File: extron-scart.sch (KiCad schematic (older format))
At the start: 6 parts, among them J1 SCART-F, J2 Conn_Coaxial, J3 Conn_Coaxial, J4 Conn_Coaxial, J5 Conn_Coaxial, J6 Conn_01x03_Male

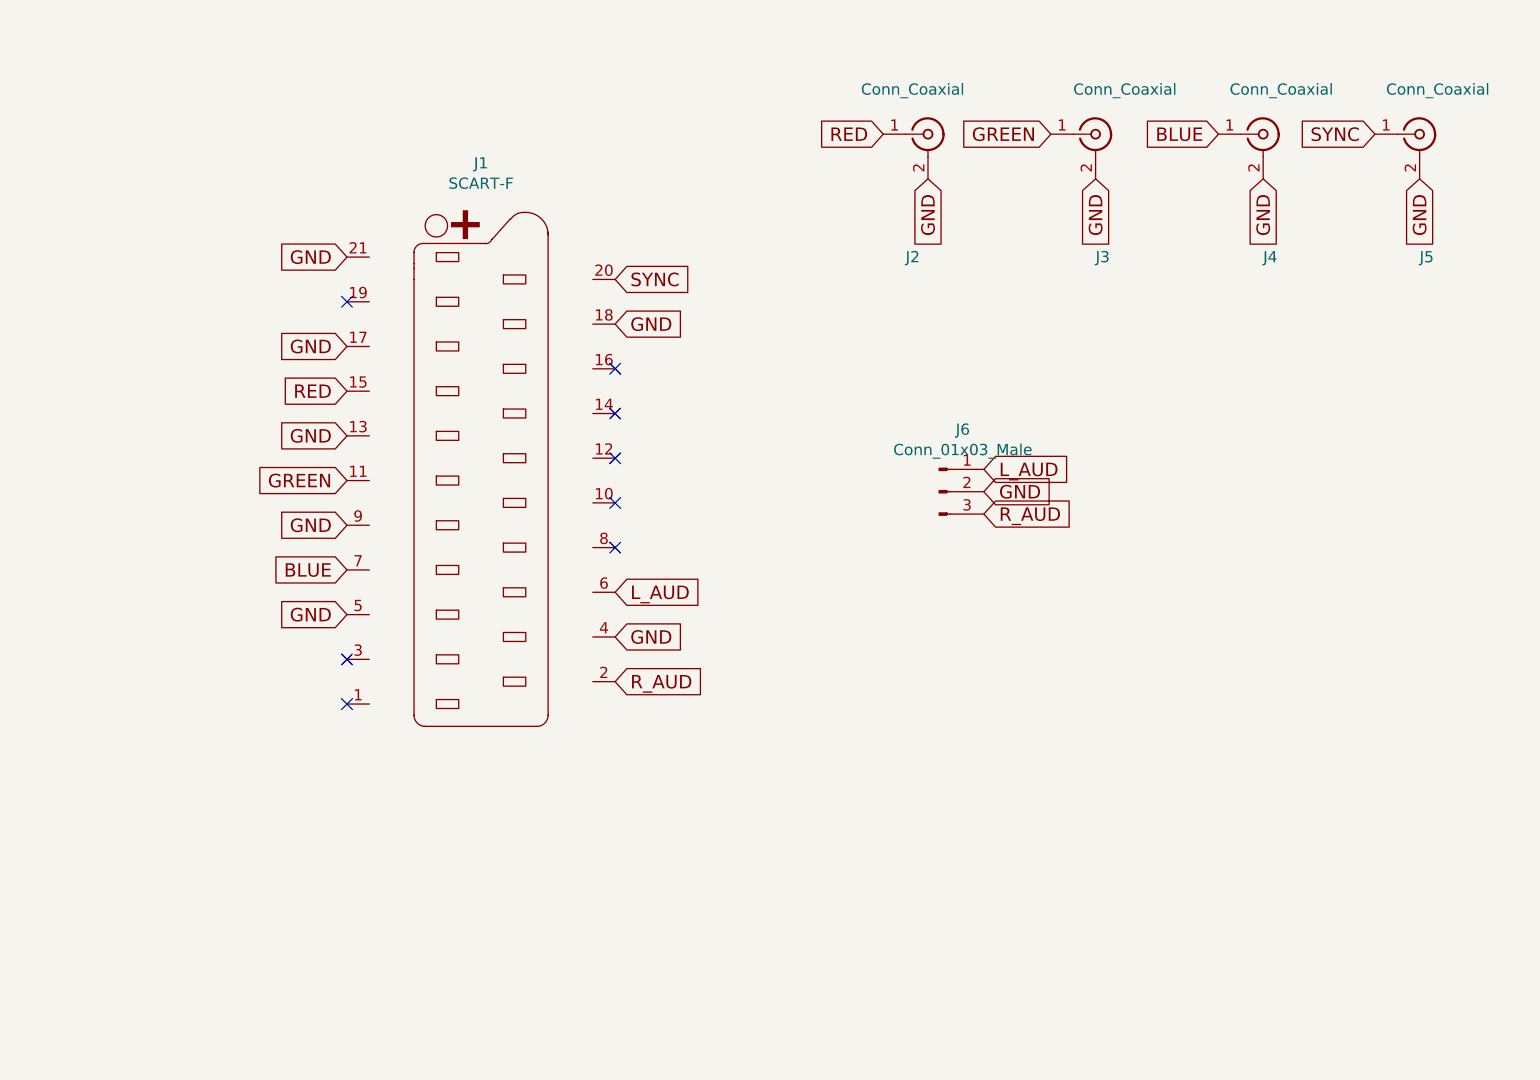
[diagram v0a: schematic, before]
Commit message: New sch/pcb input from extron crosspoint dimensions
Different orientation for the board
Added selectable sync stripper

Missing mounting holes, and better silkscreen, but mostly done
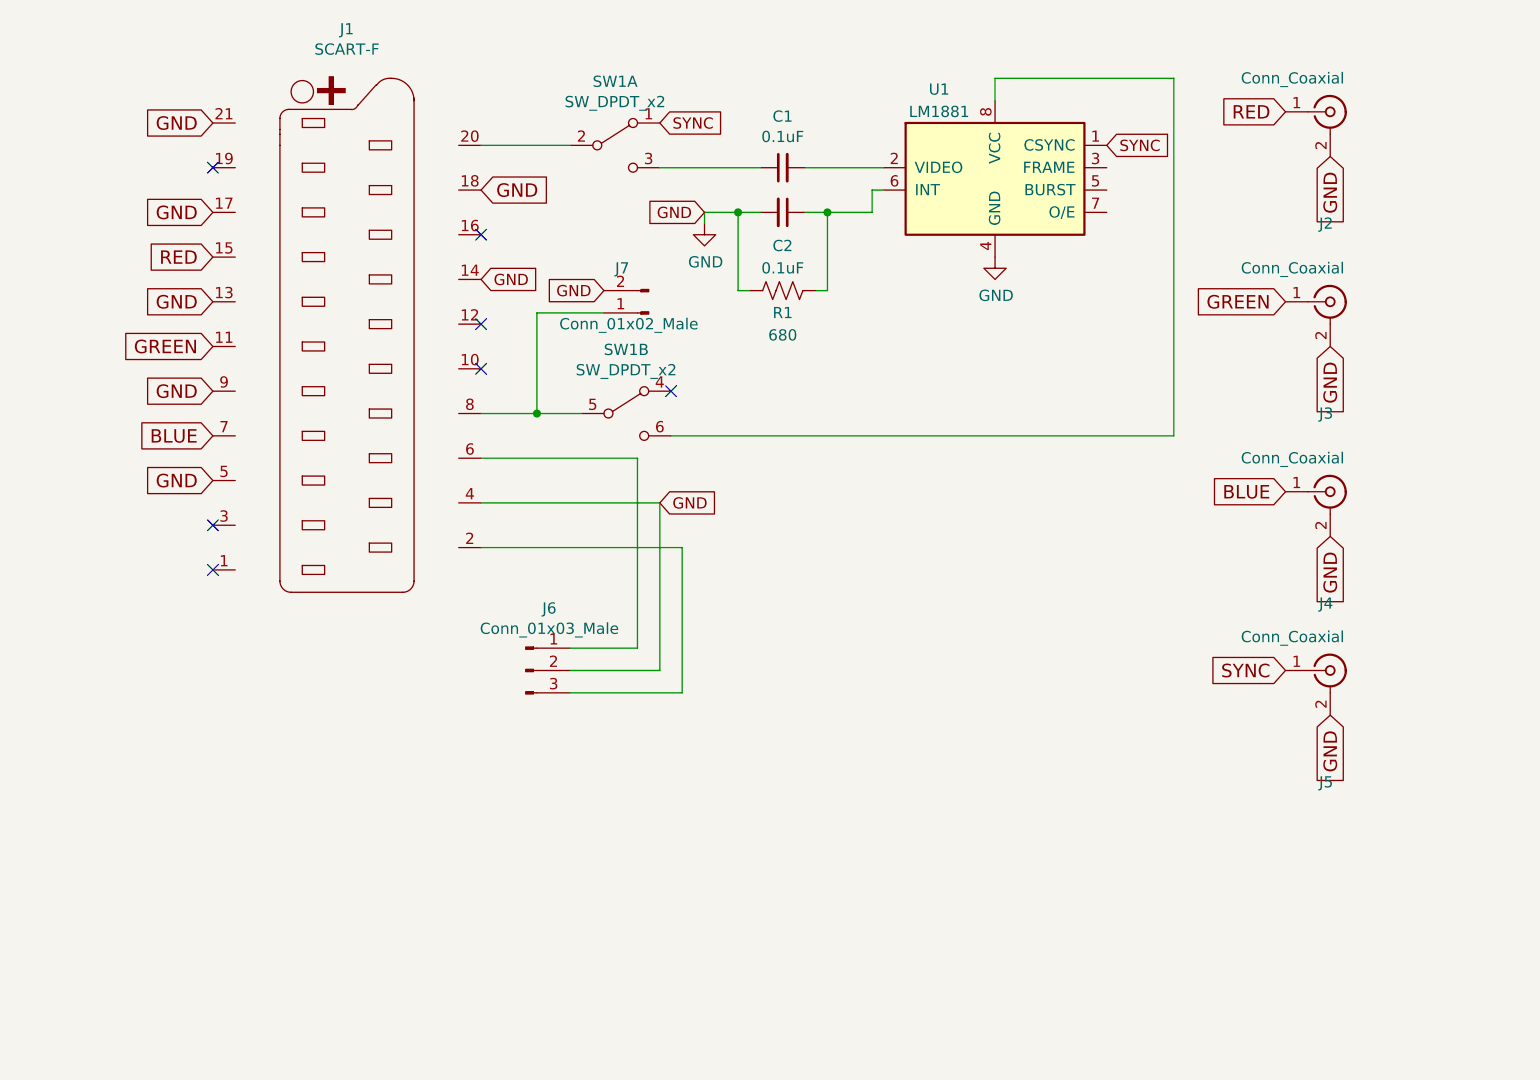
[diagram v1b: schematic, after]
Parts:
- added C1, C2: 0.1uF, Capacitor_THT:C_Disc_D3.0mm_W1.6mm_P2.50mm, symbol Device:C_Small
- added J7: Conn_01x02_Male, Connector_JST:JST_EH_B02B-EH-A_1x02_P2.50mm_Vertical, symbol Connector:Conn_01x02_Male
- added R1: 680, Resistor_THT:R_Axial_DIN0204_L3.6mm_D1.6mm_P1.90mm_Vertical, symbol Device:R_US
- added SW1: SW_DPDT_x2, Button_Switch_THT:SW_CuK_JS202011AQN_DPDT_Angled, symbol Switch:SW_DPDT_x2
- added U1: LM1881, Package_DIP:DIP-8_W7.62mm, symbol Video:LM1881
- J1: footprint extron-scart:SCART_F -> extron-scart:SCART_F_RA
- J2, J3, J4, J5: footprint extron-scart:RCA -> extron-scart:BNC_90
- J6: footprint Connector_PinHeader_2.54mm:PinHeader_1x03_P2.54mm_Vertical -> Connector_JST:JST_EH_B03B-EH-A_1x03_P2.50mm_Vertical
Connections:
- net GND: now also J1.14 (P14), C2.2, J7.2 (Pin_2), R1.1, U1.4 (GND)
- net SYNC: now also SW1.1 (A), U1.1 (CSYNC); no longer J1.20 (P20)
- net at J1.8 (P8): now also J7.1 (Pin_1), SW1.5 (B)
- net L_AUD: no longer names the net of J1.6 (P6), J6.1 (Pin_1)
- net R_AUD: no longer names the net of J1.2 (P2), J6.3 (Pin_3)
- new net: J1.20 (P20), SW1.2 (B)
- new net: C1.2, U1.2 (VIDEO)
- new net: C2.1, R1.2, U1.6 (INT)
- new net: SW1.6 (C), U1.8 (VCC)
- new net: C1.1, SW1.3 (C)
- no-connect marks 8 -> 7
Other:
- moved on the sheet: J1, J2, J3, J4, J5, J6

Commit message: V1.0 -> Sent to JLCPCB
Hopefully everything is right
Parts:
- added J10, J11, J8, J9: Conn_01x01, MountingHole:MountingHole_3.2mm_M3, symbol Connector_Generic:Conn_01x01
- J6: footprint Connector_JST:JST_EH_B03B-EH-A_1x03_P2.50mm_Vertical -> Connector_JST:JST_EH_S03B-EH_1x03_P2.50mm_Horizontal
- J7: footprint Connector_JST:JST_EH_B02B-EH-A_1x02_P2.50mm_Vertical -> Connector_JST:JST_EH_S02B-EH_1x02_P2.50mm_Horizontal
- R1: value 680 -> 680k
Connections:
- no-connect marks 7 -> 11
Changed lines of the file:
@@
 F 0 "J6" H 4756 4828 50  0000 C CNN
 F 1 "Conn_01x03_Male" H 4756 4737 50  0000 C CNN
-F 2 "Connector_JST:JST_EH_B03B-EH-A_1x03_P2.50mm_Vertical" H 4650 4550 50  0001 C CNN
+F 2 "Connector_JST:JST_EH_S03B-EH_1x03_P2.50mm_Horizontal" H 4650 4550 50  0001 C CNN
 F 3 "~" H 4650 4550 50  0001 C CNN
 	1    4650 4550
@@
 F 0 "J7" H 5350 2750 50  0000 R CNN
 F 1 "Conn_01x02_Male" H 5600 3000 50  0000 R CNN
-F 2 "Connector_JST:JST_EH_B02B-EH-A_1x02_P2.50mm_Vertical" H 5200 2950 50  0001 C CNN
+F 2 "Connector_JST:JST_EH_S02B-EH_1x02_P2.50mm_Horizontal" H 5200 2950 50  0001 C CNN
 F 3 "~" H 5200 2950 50  0001 C CNN
 	1    5200 2950
@@
 P 5800 2850
 F 0 "R1" V 5700 2850 50  0000 C CNN
-F 1 "680" V 5600 2850 50  0000 C CNN
+F 1 "680k" V 5600 2850 50  0000 C CNN
 F 2 "Resistor_THT:R_Axial_DIN0204_L3.6mm_D1.6mm_P1.90mm_Vertical" V 5840 2840 50  0001 C CNN
 F 3 "~" H 5800 2850 50  0001 C CNN
@@
 Text GLabel 5250 3800 2    50   Input ~ 0
 GND
+NoConn ~ 2400 5600
+NoConn ~ 2400 5800
+NoConn ~ 2400 6000
+NoConn ~ 2400 6200
+$Comp
+L Connector_Generic:Conn_01x01 J8
+U 1 1 5C7605B3
+P 2600 5600
+F 0 "J8" H 2680 5642 50  0000 L CNN
+F 1 "Conn_01x01" H 2680 5551 50  0000 L CNN
+F 2 "MountingHole:MountingHole_3.2mm_M3" H 2600 5600 50  0001 C CNN
+F 3 "~" H 2600 5600 50  0001 C CNN
+	1    2600 5600
+	1    0    0    -1
+$EndComp
+$Comp
+L Connector_Generic:Conn_01x01 J9
+U 1 1 5C76074F
+P 2600 5800
+F 0 "J9" H 2680 5842 50  0000 L CNN
+F 1 "Conn_01x01" H 2680 5751 50  0000 L CNN
+F 2 "MountingHole:MountingHole_3.2mm_M3" H 2600 5800 50  0001 C CNN
+F 3 "~" H 2600 5800 50  0001 C CNN
+	1    2600 5800
+	1    0    0    -1
+$EndComp
+$Comp
+L Connector_Generic:Conn_01x01 J10
+U 1 1 5C760785
+P 2600 6000
+F 0 "J10" H 2680 6042 50  0000 L CNN
+F 1 "Conn_01x01" H 2680 5951 50  0000 L CNN
+F 2 "MountingHole:MountingHole_3.2mm_M3" H 2600 6000 50  0001 C CNN
+F 3 "~" H 2600 6000 50  0001 C CNN
+	1    2600 6000
+	1    0    0    -1
+$EndComp
+$Comp
+L Connector_Generic:Conn_01x01 J11
+U 1 1 5C7607B9
+P 2600 6200
+F 0 "J11" H 2680 6242 50  0000 L CNN
+F 1 "Conn_01x01" H 2680 6151 50  0000 L CNN
+F 2 "MountingHole:MountingHole_3.2mm_M3" H 2600 6200 50  0001 C CNN
+F 3 "~" H 2600 6200 50  0001 C CNN
+	1    2600 6200
+	1    0    0    -1
+$EndComp
 $EndSCHEMATC
